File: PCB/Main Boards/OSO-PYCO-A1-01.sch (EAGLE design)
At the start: 69 parts, among them Q1 DMG341, SW1 JS102011SAQN, U1 AP7332-3333W6-7SOT23, U2 MCP73831T-2ACI/OT, U3 ATSAMD51G18A-MUT, U4 2MB Flash, U5 REG710NA-5/3K

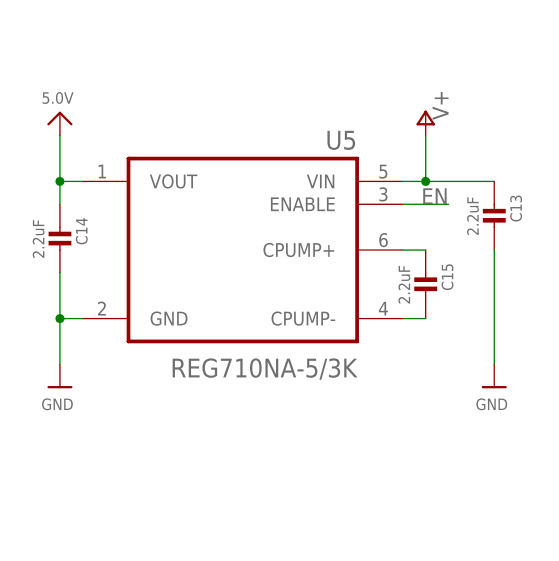
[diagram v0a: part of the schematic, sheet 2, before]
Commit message: fix capacitor value
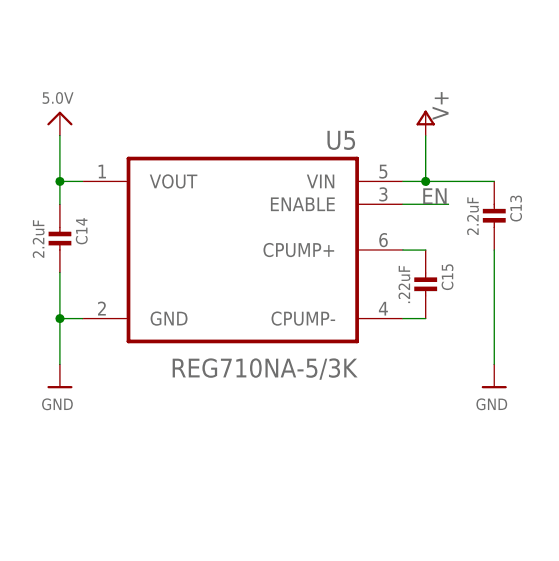
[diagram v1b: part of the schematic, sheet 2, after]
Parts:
- C15: value 2.2uF -> .22uF
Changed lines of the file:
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@@
 <part name="U5" library="REG710NA-5_3K" deviceset="REG710NA-5/3K" device=""/>
 <part name="P+2" library="supply1" library_urn="urn:adsk.eagle:library:371" deviceset="V+" device=""/>
-<part name="C15" library="microbuilder" deviceset="CAP_CERAMIC" device="_0603MP" value="2.2uF">
+<part name="C15" library="microbuilder" deviceset="CAP_CERAMIC" device="_0603MP" value=".22uF">
 <attribute name="REV" value="A"/>
 </part>
